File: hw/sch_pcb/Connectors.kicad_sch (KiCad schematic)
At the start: 16 parts

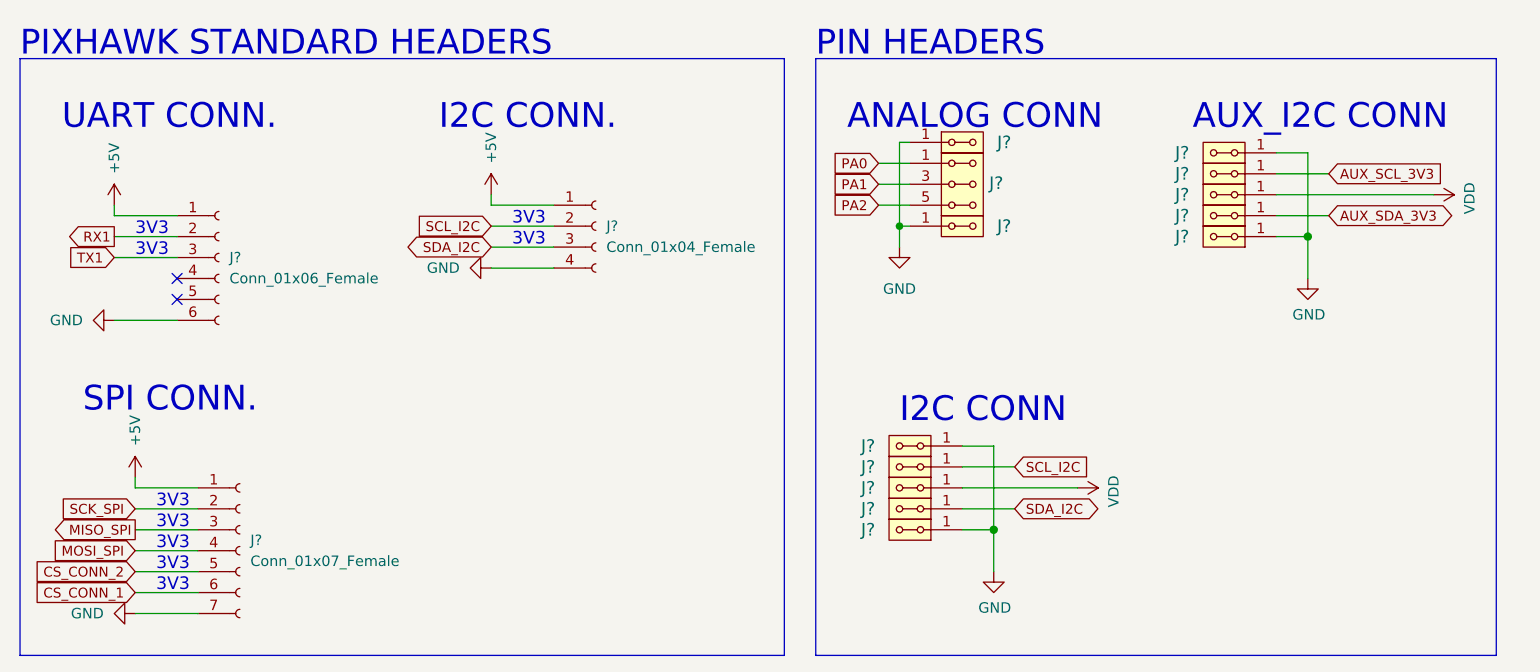
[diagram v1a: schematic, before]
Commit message: schematics update
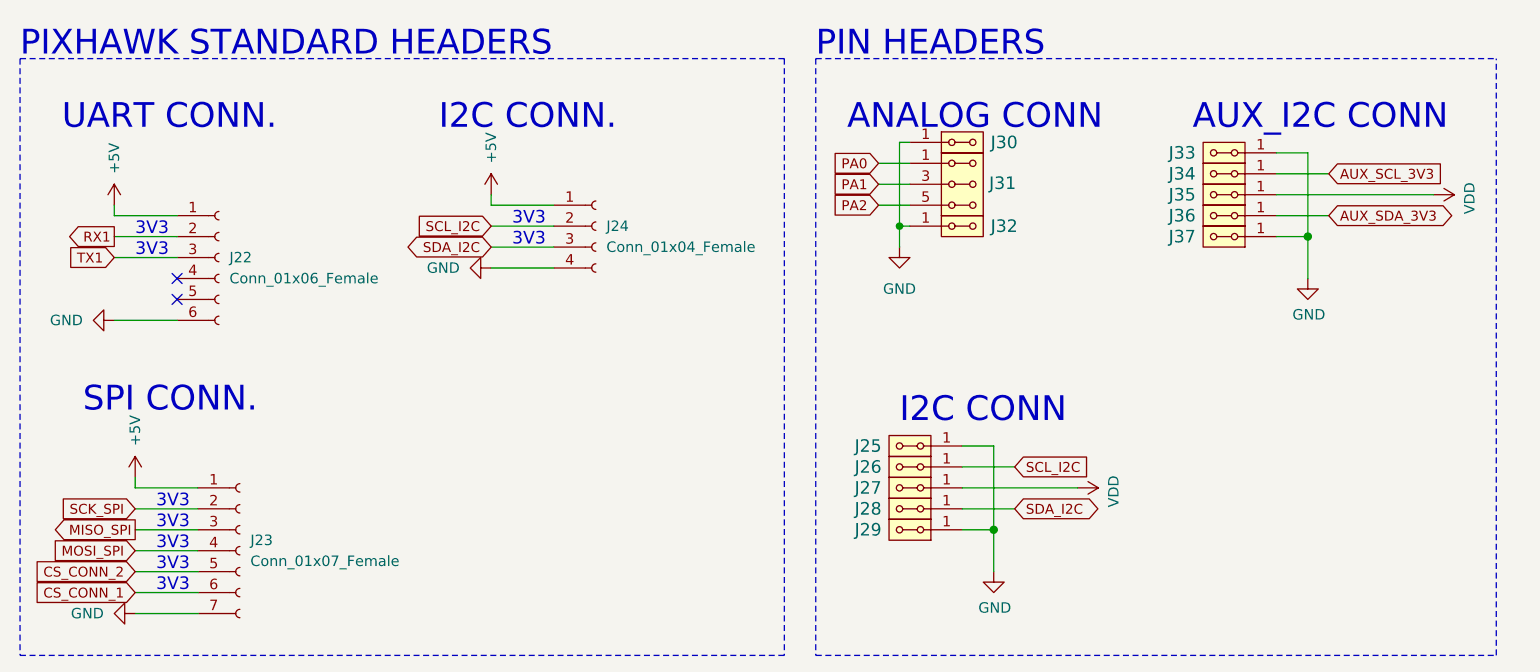
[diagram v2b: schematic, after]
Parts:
- gave numbers to parts that had none: 16

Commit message: schematics update
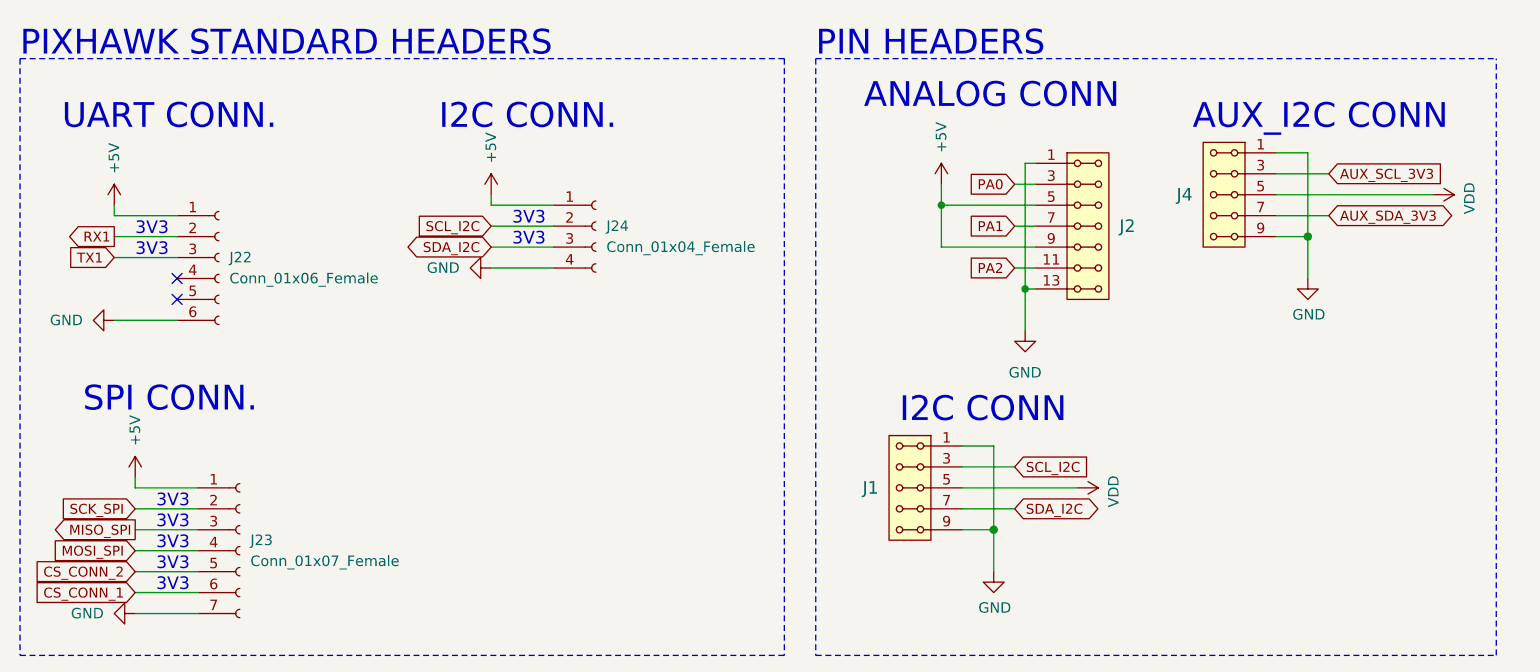
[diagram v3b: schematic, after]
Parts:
- removed J25, J26, J27, J28, J29, J30, J32, J33, J34, J35, J36, J37: HEADER_2x01_PARALLEL, Mlab_Pin_Headers:Straight_2x01, symbol DATALOGGER01A-rescue:HEADER_2x01_PARALLEL-MLAB_HEADER
- removed J31: HEADER_2x03_PARALLEL, Mlab_Pin_Headers:Straight_2x03, symbol DATALOGGER01A-rescue:HEADER_2x03_PARALLEL-MLAB_HEADER
- added J1, J4: HEADER_2x05_PARALLEL, symbol MLAB_HEADER:HEADER_2x05_PARALLEL
- added J2: HEADER_2x07_PARALLEL, symbol MLAB_HEADER:HEADER_2x07_PARALLEL
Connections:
- net +5V: now also J2.10, J2.5, J2.6, J2.9
- net AUX_SCL_3V3: now also J4.3, J4.4
- net AUX_SDA_3V3: now also J4.7, J4.8
- net GND: now also J1.1, J1.10, J1.2, J1.9, J2.1, J2.13, J2.14, J2.2, J4.1, J4.10, J4.2, J4.9
- net PA0: now also J2.3, J2.4
- net PA1: now also J2.7, J2.8
- net PA2: now also J2.11, J2.12
- net SCL_I2C: now also J1.3, J1.4
- net SDA_I2C: now also J1.7, J1.8
- net VDD: now also J1.5, J1.6, J4.5, J4.6

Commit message: progress?
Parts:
- J10: renamed from J1; footprint (none) -> Mlab_Pin_Headers:Straight_2x05
- J11: renamed from J2; footprint (none) -> Mlab_Pin_Headers:Straight_2x07
- J12: renamed from J4; footprint (none) -> Mlab_Pin_Headers:Straight_2x05
- J7: renamed from J22; footprint (none) -> Connector_JST:JST_GH_SM06B-GHS-TB_1x06-1MP_P1.25mm_Horizontal
- J8: renamed from J23; footprint (none) -> Connector_JST:JST_GH_SM07B-GHS-TB_1x07-1MP_P1.25mm_Horizontal
- J9: renamed from J24; footprint (none) -> Connector_JST:JST_GH_SM04B-GHS-TB_1x04-1MP_P1.25mm_Horizontal
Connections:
- net VDD renamed +3.3V
